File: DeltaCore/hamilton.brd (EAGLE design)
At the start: 42 x 18.3 mm, 63 parts, among them J1 CUTJ2, Q1 CSD16301Q2, Q2 CSD16301Q2, U1 SAMR21, U2 APDS9007, U3 MMA7660FC, U4 AT30TS74, U5 AT24CM02, U6 MCP73871-2AAI/ML, U7 BQ29718, U8 MCP1824ST-3302E/DB, U9 TPS61090, X1 XTAL

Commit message: updates
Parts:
- added L2: 6.8uH, insole:2-SMD-7.8-7-5
- C21: value T491C686K010AT -> 100uF
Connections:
- new net N$27: L2.P$1, U9.SW, U9.SW_2
- net OUT: now also L2.P$2
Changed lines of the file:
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@@
 <element name="R10" library="resistor" package="R0603" value="390k" x="-21.336" y="-77.47"/>
 <element name="C20" library="resistor" package="C0603" value="100nF" x="-21.336" y="-82.296"/>
-<element name="C21" library="insole" package="6032" value="T491C686K010AT" x="-18.288" y="-89.154"/>
+<element name="C21" library="insole" package="6032" value="100uF" x="-18.288" y="-89.154"/>
 <element name="C22" library="resistor" package="C0603" value="10uF" x="-21.336" y="-96.012"/>
 <element name="R11" library="resistor" package="R0603" value="1M" x="-21.336" y="-100.838"/>
+<element name="L2" library="insole" package="2-SMD-7.8-7-5" value="6.8uH" x="-26.924" y="-96.266"/>
 </elements>
 <signals>
@@
 <contactref element="C19" pad="1"/>
 <contactref element="C20" pad="1"/>
+<contactref element="L2" pad="P$2"/>
+<wire x1="-22.186" y1="-82.296" x2="-26.924" y2="-98.766" width="0" layer="19" extent="1-1"/>
 <wire x1="-20.486" y1="-72.644" x2="-22.186" y2="-82.296" width="0" layer="19" extent="1-1"/>
 <wire x1="-22.186" y1="-67.818" x2="-20.486" y2="-72.644" width="0" layer="19" extent="1-1"/>
@@
 <wire x1="-17.158" y1="-61.006" x2="-22.186" y2="-100.838" width="0" layer="19" extent="1-1"/>
 </signal>
+<signal name="N$27">
+<contactref element="U9" pad="SW_2"/>
+<contactref element="U9" pad="SW"/>
+<contactref element="L2" pad="P$1"/>
+<wire x1="-21.958" y1="-62.946" x2="-26.924" y2="-93.766" width="0" layer="19" extent="1-1"/>
+<wire x1="-21.958" y1="-62.296" x2="-21.958" y2="-62.946" width="0" layer="19" extent="1-1"/>
+</signal>
 </signals>

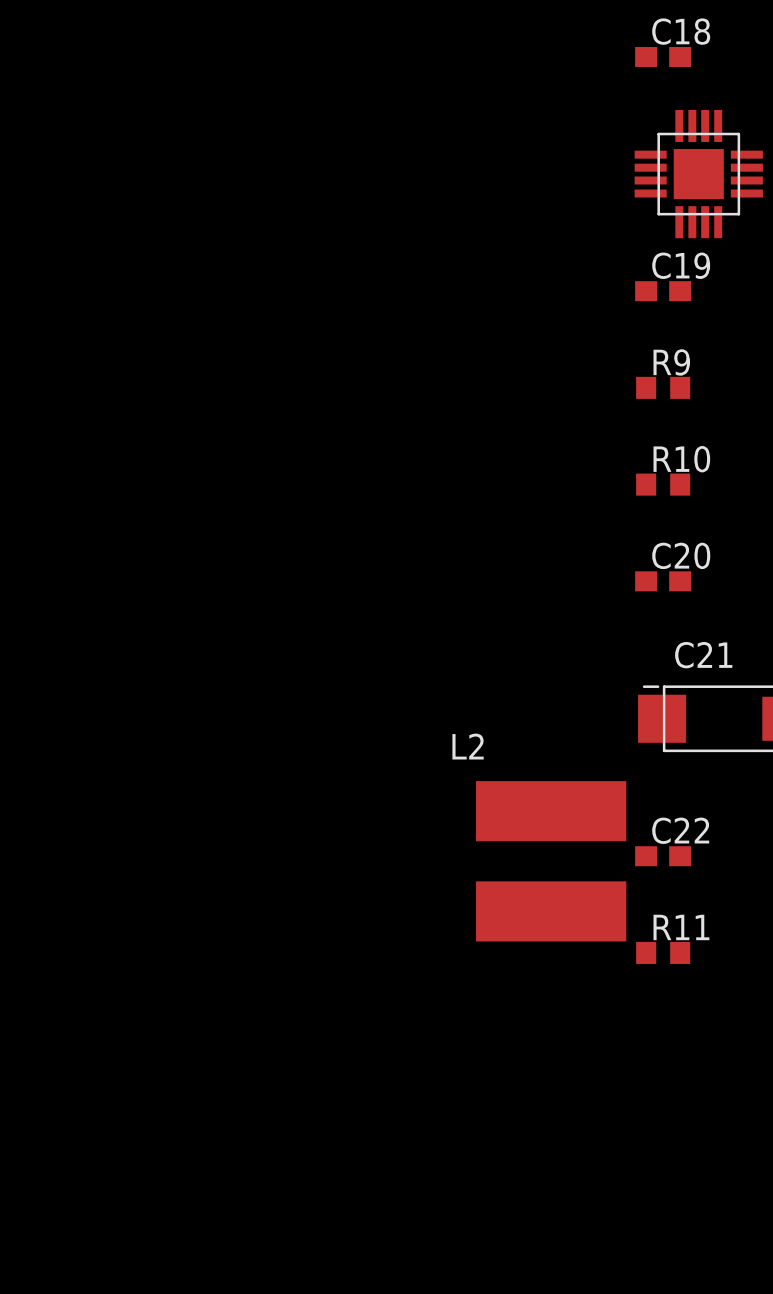
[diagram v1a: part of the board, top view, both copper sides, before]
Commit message: adding in fets, i2c expander
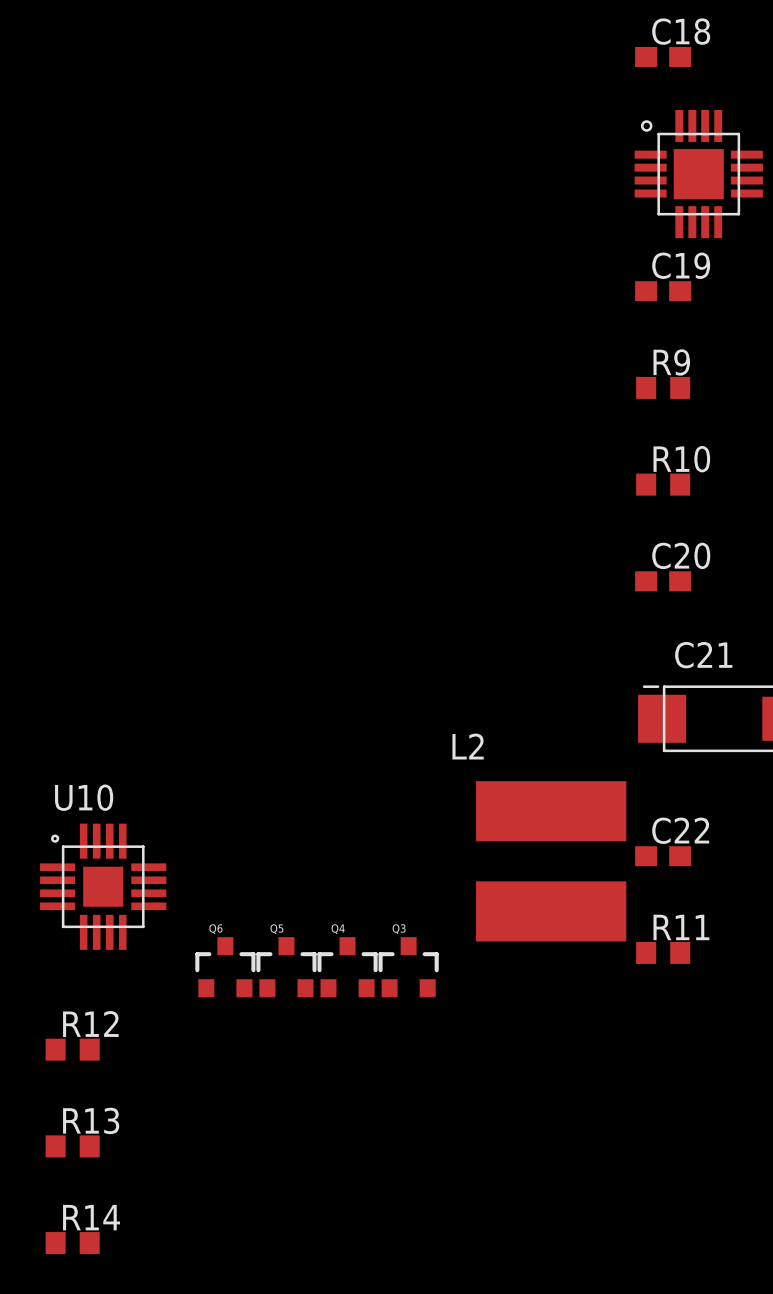
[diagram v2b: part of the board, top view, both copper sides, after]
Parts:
- added Q3, Q4, Q5, Q6: MOSFET-NCHANNEL_SOT23-3, Simplex-DiscreteSemi:SOT23-3
- added R12, R13: 1.6k, resistor:R0603
- added R14: 1.1k, resistor:R0603
- added U10: PCA9557, insole:SOT629-1
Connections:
- new net N$29: R14.1, U10.P$13
- new net N$30: Q3.1, U10.P$5
- new net N$31: Q4.1, U10.P$7
- new net N$32: Q5.1, U10.P$8
- new net N$33: Q6.1, U10.P$9
- net +3V3: now also R12.2, R13.2, R14.2, U10.P$14
- net GND: now also U10.P$1, U10.P$2, U10.P$3, U10.P$6
- net SCL: now also R12.1, U10.P$15
- net SDA: now also R13.1, U10.P$16
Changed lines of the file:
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@@
 <layer number="51" name="tDocu" color="7" fill="1" visible="no" active="yes"/>
 <layer number="52" name="bDocu" color="7" fill="1" visible="no" active="yes"/>
+<layer number="53" name="tGND_GNDA" color="7" fill="9" visible="no" active="no"/>
+<layer number="54" name="bGND_GNDA" color="1" fill="9" visible="no" active="no"/>
 <layer number="56" name="wert" color="7" fill="1" visible="no" active="no"/>
 <layer number="90" name="Modules" color="5" fill="1" visible="no" active="no"/>
@@
 <layer number="101" name="Gehäuse" color="7" fill="1" visible="no" active="yes"/>
 <layer number="102" name="Mittellin" color="7" fill="1" visible="no" active="yes"/>
+<layer number="103" name="tMap" color="7" fill="1" visible="no" active="yes"/>
 <layer number="104" name="Name" color="7" fill="1" visible="no" active="yes"/>
+<layer number="105" name="tPlate" color="7" fill="1" visible="no" active="yes"/>
+<layer number="106" name="bPlate" color="7" fill="1" visible="no" active="yes"/>
+<layer number="107" name="Crop" color="7" fill="1" visible="no" active="yes"/>
+<layer number="116" name="Patch_BOT" color="9" fill="4" visible="no" active="yes"/>
+<layer number="121" name="_tsilk" color="7" fill="1" visible="no" active="yes"/>
+<layer number="122" name="_bsilk" color="7" fill="1" visible="no" active="yes"/>
+<layer number="125" name="_tNames" color="7" fill="1" visible="no" active="yes"/>
+<layer number="144" name="Drill_legend" color="7" fill="1" visible="no" active="yes"/>
 <layer number="151" name="HeatSink" color="7" fill="1" visible="no" active="yes"/>
 <layer number="200" name="200bmp" color="1" fill="10" visible="no" active="yes"/>
 <layer number="201" name="201bmp" color="2" fill="10" visible="no" active="yes"/>
+<layer number="202" name="202bmp" color="3" fill="10" visible="no" active="yes"/>
+<layer number="203" name="203bmp" color="4" fill="10" visible="no" active="yes"/>
+<layer number="204" name="204bmp" color="5" fill="10" visible="no" active="yes"/>
+<layer number="205" name="205bmp" color="6" fill="10" visible="no" active="yes"/>
+<layer number="206" name="206bmp" color="7" fill="10" visible="no" active="yes"/>
+<layer number="207" name="207bmp" color="8" fill="10" visible="no" active="yes"/>
+<layer number="208" name="208bmp" color="9" fill="10" visible="no" active="yes"/>
+<layer number="209" name="209bmp" color="7" fill="1" visible="no" active="yes"/>
+<layer number="210" name="210bmp" color="7" fill="1" visible="no" active="yes"/>
+<layer number="211" name="211bmp" color="7" fill="1" visible="no" active="yes"/>
+<layer number="212" name="212bmp" color="7" fill="1" visible="no" active="yes"/>
+<layer number="213" name="213bmp" color="7" fill="1" visible="no" active="yes"/>
+<layer number="214" name="214bmp" color="7" fill="1" visible="no" active="yes"/>
+<layer number="215" name="215bmp" color="7" fill="1" visible="no" active="yes"/>
+<layer number="216" name="216bmp" color="7" fill="1" visible="no" active="yes"/>
+<layer number="217" name="217bmp" color="18" fill="1" visible="no" active="no"/>
+<layer number="218" name="218bmp" color="19" fill="1" visible="no" active="no"/>
+<layer number="219" name="219bmp" color="20" fill="1" visible="no" active="no"/>
+<layer number="220" name="220bmp" color="21" fill="1" visible="no" active="no"/>
+<layer number="221" name="221bmp" color="22" fill="1" visible="no" active="no"/>
+<layer number="222" name="222bmp" color="23" fill="1" visible="no" active="no"/>
+<layer number="223" name="223bmp" color="24" fill="1" visible="no" active="no"/>
+<layer number="224" name="224bmp" color="25" fill="1" visible="no" active="no"/>
 <layer number="250" name="Descript" color="7" fill="1" visible="no" active="yes"/>
 <layer number="251" name="SMDround" color="7" fill="1" visible="no" active="yes"/>
@@
 <element name="R11" library="resistor" package="R0603" value="1M" x="-21.336" y="-100.838"/>
 <element name="L2" library="insole" package="2-SMD-7.8-7-5" value="6.8uH" x="-26.924" y="-96.266"/>
+<element name="Q3" library="Simplex-DiscreteSemi" package="SOT23-3" value="MOSFET-NCHANNEL_SOT23-3" x="-34.036" y="-101.6"/>
+<element name="Q4" library="Simplex-DiscreteSemi" package="SOT23-3" value="MOSFET-NCHANNEL_SOT23-3" x="-37.084" y="-101.6"/>
+<element name="Q5" library="Simplex-DiscreteSemi" package="SOT23-3" value="MOSFET-NCHANNEL_SOT23-3" x="-40.132" y="-101.6"/>
+<element name="Q6" library="Simplex-DiscreteSemi" package="SOT23-3" value="MOSFET-NCHANNEL_SOT23-3" x="-43.18" y="-101.6"/>
+<element name="U10" library="insole" package="SOT629-1" value="PCA9557" x="-49.276" y="-97.536"/>
+<element name="R12" library="resistor" package="R0603" value="1.6k" x="-50.8" y="-105.664"/>
+<element name="R13" library="resistor" package="R0603" value="1.6k" x="-50.8" y="-110.49"/>
+<element name="R14" library="resistor" package="R0603" value="1.1k" x="-50.8" y="-115.316"/>
 </elements>
 <signals>
@@
 <contactref element="C22" pad="2"/>
 <contactref element="C21" pad="CATHODE"/>
+<contactref element="U10" pad="P$1"/>
+<contactref element="U10" pad="P$2"/>
+<contactref element="U10" pad="P$3"/>
+<contactref element="U10" pad="P$6"/>
+<wire x1="-51.551" y1="-97.211" x2="-51.551" y2="-96.561" width="0" layer="19" extent="1-1"/>
+<wire x1="-51.551" y1="-97.861" x2="-51.551" y2="-97.211" width="0" layer="19" extent="1-1"/>
+<wire x1="-49.601" y1="-99.811" x2="-51.551" y2="-97.861" width="0" layer="19" extent="1-1"/>
+<wire x1="-20.486" y1="-96.012" x2="-49.601" y2="-99.811" width="0" layer="19" extent="1-1"/>
 <wire x1="-21.388" y1="-89.154" x2="-20.486" y2="-96.012" width="0" layer="19" extent="1-1"/>
 <wire x1="-20.486" y1="-82.296" x2="-21.388" y2="-89.154" width="0" layer="19" extent="1-1"/>
@@
 <contactref element="U8" pad="3"/>
 <contactref element="C18" pad="1"/>
+<contactref element="R14" pad="2"/>
+<contactref element="R13" pad="2"/>
+<contactref element="R12" pad="2"/>
+<contactref element="U10" pad="P$14"/>
+<wire x1="-49.95" y1="-110.49" x2="-49.95" y2="-115.316" width="0" layer="19" extent="1-1"/>
+<wire x1="-49.95" y1="-105.664" x2="-49.95" y2="-110.49" width="0" layer="19" extent="1-1"/>
+<wire x1="-48.951" y1="-95.261" x2="-49.95" y2="-105.664" width="0" layer="19" extent="1-1"/>
+<wire x1="-22.186" y1="-56.134" x2="-48.951" y2="-95.261" width="0" layer="19" extent="1-1"/>
 <wire x1="-19.4564" y1="-49.5554" x2="-22.186" y2="-56.134" width="0" layer="19" extent="1-1"/>
 <wire x1="12.754" y1="14.678" x2="-19.4564" y2="-49.5554" width="0" layer="19" extent="1-1"/>
@@
 <wire x1="13.462" y1="13.462" x2="14.478" y2="12.446" width="0.1524" layer="1"/>
 <wire x1="14.478" y1="12.446" x2="16.002" y2="12.446" width="0.1524" layer="1"/>
+<contactref element="U10" pad="P$16"/>
+<contactref element="R13" pad="1"/>
+<wire x1="-50.251" y1="-95.261" x2="-51.65" y2="-110.49" width="0" layer="19" extent="1-1"/>
+<wire x1="11.938" y1="13.462" x2="-50.251" y2="-95.261" width="0" layer="19" extent="1-1"/>
 </signal>
 <signal name="SCL">
@@
 <wire x1="15.494" y1="13.97" x2="15.494696875" y2="13.97" width="0.1524" layer="1"/>
 <wire x1="15.494696875" y1="13.97" x2="15.495225" y2="13.969471875" width="0.1524" layer="1"/>
+<contactref element="U10" pad="P$15"/>
+<contactref element="R12" pad="1"/>
+<wire x1="-49.601" y1="-95.261" x2="-51.65" y2="-105.664" width="0" layer="19" extent="1-1"/>
+<wire x1="13.716" y1="13.716" x2="-49.601" y2="-95.261" width="0" layer="19" extent="1-1"/>
 </signal>
 <signal name="LS">
@@
 <wire x1="-21.958" y1="-62.296" x2="-21.958" y2="-62.946" width="0" layer="19" extent="1-1"/>
 </signal>
+<signal name="N$29">
+<contactref element="U10" pad="P$13"/>
+<contactref element="R14" pad="1"/>
+<wire x1="-48.301" y1="-95.261" x2="-51.65" y2="-115.316" width="0" layer="19" extent="1-1"/>
+</signal>
+<signal name="N$30">
+<contactref element="Q3" pad="1"/>
+<contactref element="U10" pad="P$5"/>
+<wire x1="-34.986" y1="-102.6" x2="-50.251" y2="-99.811" width="0" layer="19" extent="1-1"/>
+</signal>
+<signal name="N$31">
+<contactref element="Q4" pad="1"/>
+<contactref element="U10" pad="P$7"/>
+<wire x1="-38.034" y1="-102.6" x2="-48.951" y2="-99.811" width="0" layer="19" extent="1-1"/>
+</signal>
+<signal name="N$32">
+<contactref element="Q5" pad="1"/>
+<contactref element="U10" pad="P$8"/>
+<wire x1="-41.082" y1="-102.6" x2="-48.301" y2="-99.811" width="0" layer="19" extent="1-1"/>
+</signal>
+<signal name="N$33">
+<contactref element="Q6" pad="1"/>
+<contactref element="U10" pad="P$9"/>
+<wire x1="-47.001" y1="-98.511" x2="-44.13" y2="-102.6" width="0" layer="19" extent="1-1"/>
+</signal>
 </signals>

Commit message: update
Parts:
- removed BT1: 2/3A, storm:2/3A
- removed D1: SOD523F, storm:SOD523F
- removed D2: DNP, storm:LINE_0805
- removed GND, UNREG, VCC: (no value), wirepad:SMD1,27-2,54
- removed J1: CUTJ2, storm:CUT3
- removed R4: DNP, storm:S0402
- removed TP1: D19, storm:TPP
- removed TP2: D18, storm:TPP
- removed TP3: AN7, storm:TPP
- removed TP4: D25, storm:TPP
- removed TP7: SDA, storm:TPP
- removed TP8: SCL, storm:TPP
- removed U6: MCP73871-2AAI/ML, Microchip_By_element14_Batch_1:QFN50P400X400X100-21N
- added JP2: insole1, pinhead:1X02
- added JP3: insole2, pinhead:1X02
- added JP4: insole3, pinhead:1X02
- added JP5: insole4, pinhead:1X02
- added JP6: insole/wrist, pinhead:1X02
- added JP7: insole/fan/pwm, pinhead:1X03
- added JP8: PRU input, pinhead:1X03
- added Q7, Q8: NFET_AON7408, fets:VDFN3X38L
- Q1, Q2: value CSD16301Q2 -> (none)
- U5: value AT24CM02 -> MCP73871-2AAI/ML; device storm:SO8 -> Microchip_By_element14_Batch_1:QFN50P400X400X100-21N
- moved Q6 144.4 mm to (27.4, 24.4), flipped to the bottom, turned to 90 degrees
- moved R14 141.0 mm to (8.38, 12.7), flipped to the bottom
- moved Q5 140.9 mm to (22.9, 24.4), flipped to the bottom, turned to 90 degrees
- moved R13 140.8 mm to (8.38, 17.3), flipped to the bottom
- moved Q4 137.5 mm to (18.0, 24.4), flipped to the bottom, turned to 90 degrees
- moved Q3 134.7 mm to (13.7, 24.4), flipped to the bottom, turned to 90 degrees
- moved R12 134.0 mm to (7.62, 15.0), flipped to the bottom, turned to 270 degrees
- moved R11 131.2 mm to (20.1, 23.6)
- moved U10 128.1 mm to (11.9, 15.0), flipped to the bottom, turned to 270 degrees
- moved C22 127.5 mm to (10.4, 27.4), turned to 270 degrees
- moved L2 125.5 mm to (4.83, 25.1)
- moved R10 110.9 mm to (20.1, 25.4), turned to 180 degrees
- moved C21 110.7 mm to (5.08, 19.1), turned to 180 degrees
- moved C20 109.0 mm to (20.1, 18.5)
- moved R9 103.2 mm to (20.1, 21.8)
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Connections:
- removed net N$1: BT1.POS, D1.POS, J1.P$2
- removed net N$11: D2.NOLINE, TP1.P$1, U1.20
- removed net N$12: TP2.P$1, U1.19
- removed net N$15: C14.1, U6.18, U6.19, VCC.1
- removed net N$17: U6.17, U6.3, U6.4, U6.9
- removed net N$8: TP3.P$1, U1.8
- removed net N$9: TP4.P$1, U1.23
- new net D25: JP7.3, U1.23
- new net N$34: JP3.2, Q4.2
- new net N$35: JP4.2, Q5.2
- new net N$36: JP5.2, Q6.2
- new net N$37: JP6.2, Q7.1, Q7.2, Q7.3
- new net N$39: JP7.2, Q8.1, Q8.2, Q8.3
- new net N$40: Q7.4, U10.P$10
- new net N$41: Q8.4, U10.P$11
- new net RECT: JP8.1
- new net VCC: C14.1, JP8.3, U5.18, U5.19
- net +3V3: no longer D1.NEG, J1.P$1, U5.8
- net 5V: now also JP2.1, JP3.1, JP4.1, JP5.1, JP6.1, JP7.1, U5.17, U5.3, U5.4, U5.9
- net GND: now also JP8.2, Q3.3, Q4.3, Q5.3, Q6.3, Q7.5, Q7.6, Q7.7, Q7.8, Q7.PAD, Q8.5, Q8.6, Q8.7, Q8.8, Q8.PAD, U5.10, U5.11, U5.21; no longer BT1.NEG, GND.1, R4.P$1, U5.3, U5.4, U5.7, U6.10, U6.11, U6.21
- net N$14: now also JP2.2, Q3.2; no longer D2.LINE, R4.P$2
- net N$16: now also U5.12; no longer U6.12
- net N$18: now also U5.13; no longer U6.13
- net N$19: now also U5.5; no longer U6.5
- net N$20: now also U5.14, U5.15, U5.16; no longer U6.14, U6.15, U6.16
- net OUT: now also U5.1, U5.20; no longer U6.1, U6.20
- net SCL: no longer TP8.P$1, U5.6
- net SDA: no longer TP7.P$1, U5.5
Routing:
- net SDA: track 59.8 -> 0.00 mm, vias 2 -> 0
- net SCL: track 54.6 -> 0.00 mm, vias 2 -> 0
- net N$11: track 48.7 -> 0.00 mm, vias 1 -> 0
- net N$12: track 41.5 -> 0.00 mm, vias 1 -> 0
- net N$8: track 34.0 -> 0.00 mm, vias 1 -> 0
- net N$9: track 33.7 -> 0.00 mm, vias 1 -> 0
- net +3V3: track 46.7 -> 33.9 mm, vias 10 -> 6
- net GND: track 71.1 -> 60.5 mm, vias 46 -> 43
- net N$1: track 5.15 -> 0.00 mm
- net N$14: track 2.39 -> 0.00 mm
- removed copper zone on layer 15, net +3V3
- removed copper zone on layer 2, net GND
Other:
- board size 42 x 18.3 mm -> 40 x 30 mm
- board text removed: "+"
- board text removed: "-"
- board text removed: "HAMILTON"
- board text removed: "M ANDERSEN"
- board text removed: "UC BERKELEY"

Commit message: more board
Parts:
- moved A1 37.4 mm to (43.3, 38.4), turned to 90 degrees
- moved JP7 35.9 mm to (3.56, 13.0), turned to 68.5 degrees
- moved C13 34.4 mm to (39.9, 39.3), turned to 270 degrees
- moved U4 32.8 mm to (37.9, 39.6), turned to 270 degrees
- moved JP6 32.3 mm to (5.89, 18.9), turned to 68.5 degrees
- moved C12 31.4 mm to (43.5, 19.6), turned to 90 degrees
- moved R14 30.1 mm to (25.4, 37.5), flipped to the top, turned to 90 degrees
- moved JP1 30.0 mm to (42.9, 3.51), turned to 270 degrees
- moved R12 29.1 mm to (23.1, 39.6), flipped to the top, turned to 0 degrees
- moved L1 28.5 mm to (40.5, 30.2), turned to 270 degrees
- moved C5 28.3 mm to (35.6, 37.7), turned to 180 degrees
- moved Q2 27.5 mm to (34.3, 2.27), turned to 90 degrees
- moved U3 26.5 mm to (39.9, 19.7), turned to 90 degrees
- moved C9 25.4 mm to (34.8, 35.5), turned to 270 degrees
- moved Q8 24.8 mm to (8.89, 13.5), flipped to the top
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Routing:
- net GND: track 60.5 -> 248.1 mm
- net 5V: track 0.00 -> 97.7 mm, vias 0 -> 3
- net OUT: track 0.00 -> 62.7 mm, vias 0 -> 2
- net SDA: track 0.00 -> 51.4 mm, vias 0 -> 3
- net SCL: track 0.00 -> 50.1 mm, vias 0 -> 2
- net D25: track 0.00 -> 45.4 mm, vias 0 -> 2
- net N$41: track 0.00 -> 38.8 mm, vias 0 -> 2
- net N$20: track 0.00 -> 34.1 mm
- net N$40: track 0.00 -> 28.6 mm, vias 0 -> 2
- net +3V3: track 33.9 -> 60.3 mm, vias 6 -> 10
- net N$25: track 0.00 -> 24.9 mm, vias 0 -> 1
- net N$32: track 0.00 -> 21.2 mm, vias 0 -> 2
- net N$33: track 0.00 -> 17.3 mm, vias 0 -> 2
- net N$27: track 0.00 -> 17.0 mm
- net VCC: track 0.00 -> 12.5 mm
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- added copper zone on layer 15, net +3V3
- added copper zone on layer 2, net GND
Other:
- board size 40 x 30 mm -> 45 x 41 mm

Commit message: hopefully done routing
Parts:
- added R15, R4: ??, resistor:R0603
- moved Q5 12.5 mm to (18.3, 16.2)
- moved Q6 7.97 mm to (14.7, 16.2)
- moved C21 7.87 mm to (15.0, 26.0), turned to 90 degrees
- moved U4 5.59 mm to (32.3, 39.6)
- moved C13 4.83 mm to (35.1, 39.7), turned to 0 degrees
- moved U$2 3.93 mm to (8.46, 5.59), turned to 0 degrees
- moved U5 3.06 mm to (13.4, 7.61)
- moved Q8 2.40 mm to (10.2, 15.5)
- moved L2 2.15 mm to (22.5, 25.8)
- moved Q4 1.94 mm to (16.9, 33.1)
- moved Q7 1.61 mm to (11.2, 20.1)
- moved R13 1.41 mm to (19.8, 38.5)
- moved C14 1.27 mm to (5.57, 7.79)
- moved U10 1.04 mm to (22.8, 34.4)
- moved Q3 0.79 mm to (17.2, 36.8)
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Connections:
- new net N$1: R15.2, R4.1, U5.2
- net +3V3: now also U5.17, U5.3, U5.4, U5.9
- net 5V: no longer U5.17, U5.3, U5.4, U5.9
- net GND: now also R15.1
- net RECT: now also R4.2
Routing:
- net GND: track 248.1 -> 219.0 mm, vias 43 -> 60
- net OUT: track 62.7 -> 81.8 mm
- net N$1: track 0.00 -> 17.1 mm, vias 0 -> 2
- net N$35: track 2.56 -> 15.9 mm
- net N$36: track 2.64 -> 12.2 mm, vias 0 -> 1
- net +3V3: track 60.3 -> 68.4 mm, vias 10 -> 13
- net N$41: track 38.8 -> 33.0 mm
- net SDA: track 51.4 -> 45.9 mm, vias 3 -> 4
- net VCC: track 12.5 -> 17.8 mm
- net D25: track 45.4 -> 40.8 mm, vias 2 -> 1
- net RECT: track 0.00 -> 4.56 mm
- net N$40: track 28.6 -> 24.2 mm
- net 5V: track 97.7 -> 93.5 mm, vias 3 -> 2
- net N$32: track 21.2 -> 17.1 mm
- net N$33: track 17.3 -> 20.1 mm
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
